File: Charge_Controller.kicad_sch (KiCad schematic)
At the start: 146 parts, among them J1 SOLAR, J10 Conn_01x01_Female, J11 Conn_01x01_Female, J12 Conn_01x01_Female, J13 Conn_01x01_Female, J14 Conn_01x01_Female, J15 Conn_01x01_Female, J16 Conn_01x01_Female, J17 Conn_01x01_Female, J18 Conn_01x01_Female, J19 Conn_01x01_Female, J2 Conn_01x01_Female, J20 Conn_01x01_Female, J21 Conn_01x01_Female, J22 Conn_01x01_Female, J23 Conn_01x01_Female, J24 Conn_01x01_Female, J25 Conn_01x01_Female, J26 Conn_01x01_Female, J27 Conn_01x01_Female, J28 Conn_01x01_Female, J29 Conn_01x01_Female, J3 Conn_01x01_Female, J30 Conn_01x01_Female, J31 Conn_01x01_Female, J32 Conn_01x01_Female, J36 FAN, J37 I2C_CON, J38 I2C_CON, J4 Conn_01x01_Female, J5 Conn_01x01_Female, J6 Conn_01x01_Female, J7 Conn_01x01_Female, J8 BATT, J9 USB_OTG, Q1 CSD19505, Q2 CSD19505, Q3 CSD19505, Q4 Si2306, Q5 2N3904, Q6 2N3904, Q7 PMOS-100V-78A, Q8 PMOS-100V-78A, Q9 Si2306, SW1 RIGHT, SW2 LEFT, SW3 BACK, SW4 SELECT, U1 ACS712-30A, U10 ADS1015, U11 NUP4202, U2 B1212, U3 AMS1117-5.0, U4 AMS1117-3.3, U5 XL7005A, U6 XL7005A, U7 IR2104, U8 ESP32-WROOM-32, U9 CH340C

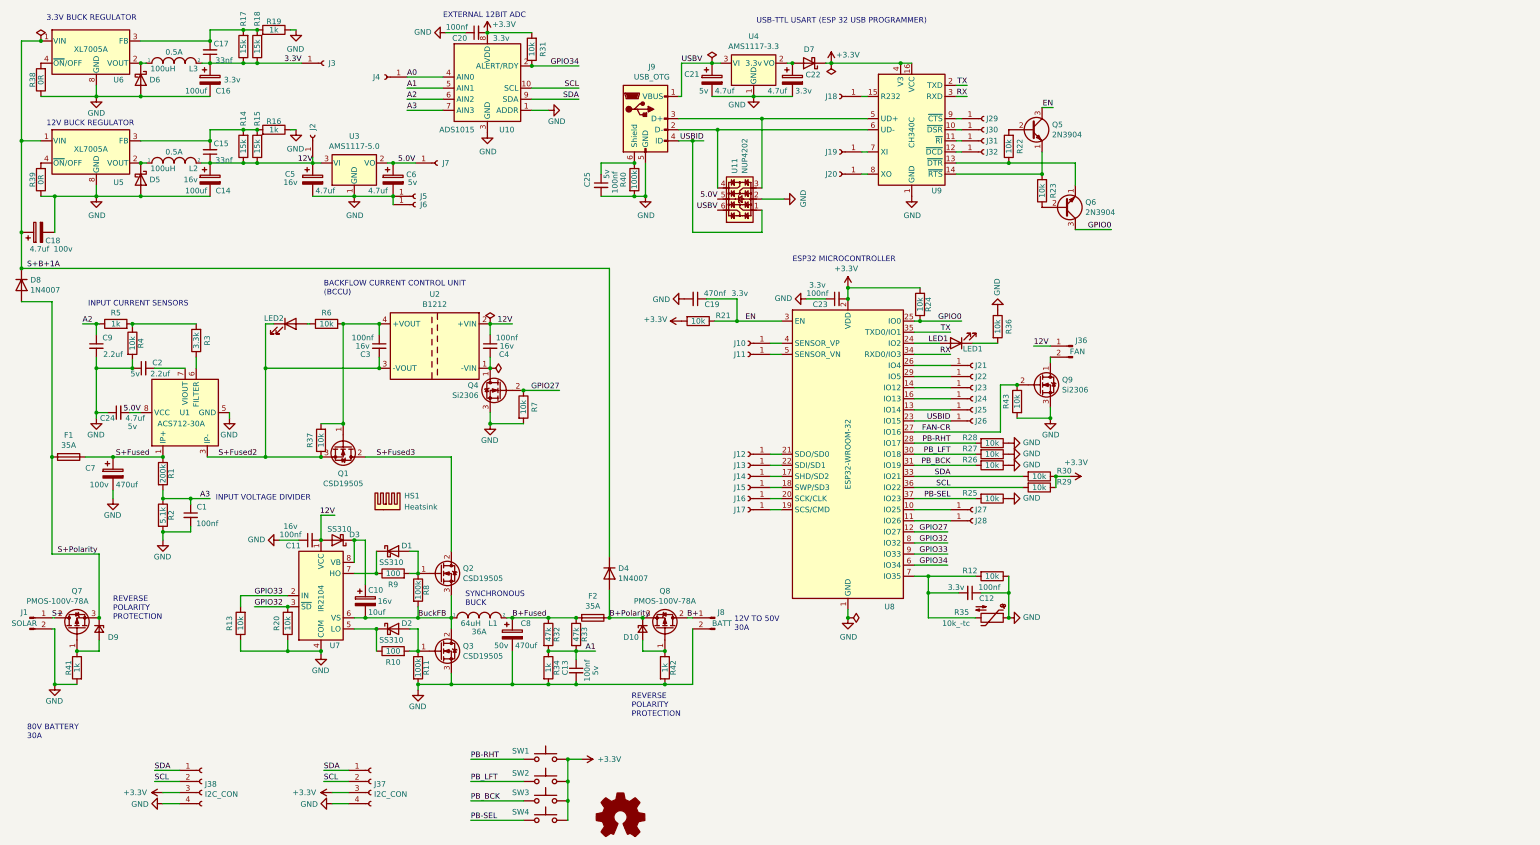
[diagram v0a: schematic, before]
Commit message: Draft adding I2C to LCD driver.
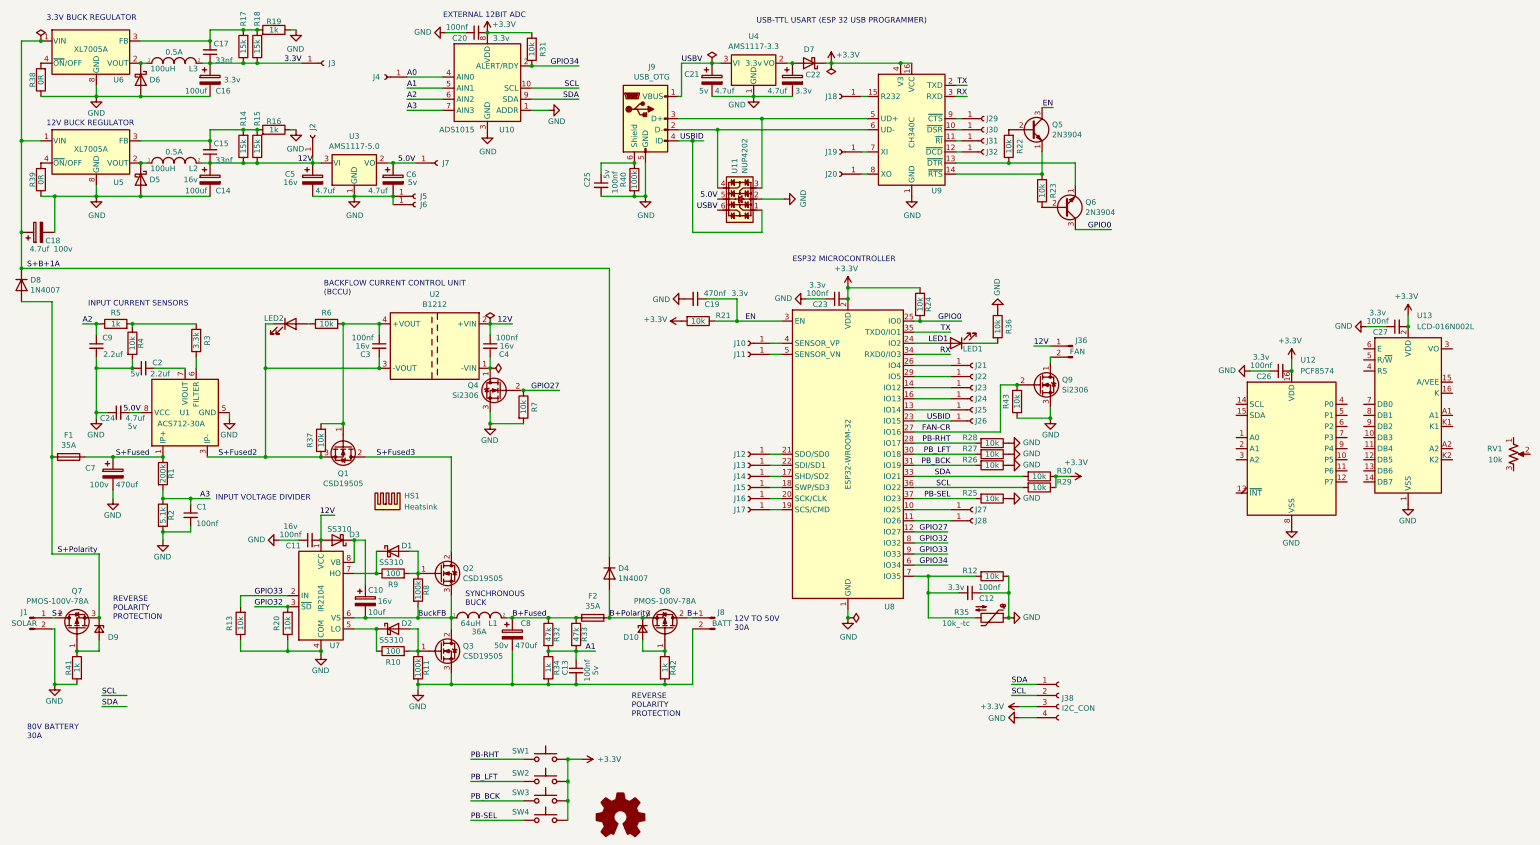
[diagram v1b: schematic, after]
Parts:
- removed J37: I2C_CON, Connector_PinHeader_2.54mm:PinHeader_1x04_P2.54mm_Vertical, symbol Connector:Conn_01x04_Female
- added C26, C27: 100nf, Capacitor_SMD:C_0805_2012Metric, symbol Device:C_Small
- added RV1: 10k, Potentiometer_SMD:Potentiometer_Bourns_3314G_Vertical, symbol Device:R_Potentiometer_US
- added U12: PCF8574, Package_SO:SSOP-20_4.4x6.5mm_P0.65mm, symbol Interface_Expansion:PCF8574
- added U13: LCD-016N002L, Display:LCD-016N002L, symbol Display_Character:LCD-016N002L
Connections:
- net +3.3VA: now also C26.2, C27.2, U12.16 (VDD), U13.2 (VDD)
- net GND: now also C26.1, C27.1, U12.8 (VSS), U13.1 (VSS)
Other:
- moved on the sheet: J38

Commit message: R0.1 almost done draft.
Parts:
- removed U13: LCD-016N002L, Display:LCD-016N002L, symbol Display_Character:LCD-016N002L
- added DS1: LCD, LCD:LCD_LCM-S01602DTR_A, symbol LCM-S01602DTR_A:LCM-S01602DTR/A
- added J33, J34: Conn_01x01_Female, TestPoint:TestPoint_Loop_D3.50mm_Drill0.9mm_Beaded, symbol Connector:Conn_01x01_Female
- added R46, R47, R48: 10k, Resistor_SMD:R_0805_2012Metric, symbol Device:R
- added R49: 330, Resistor_SMD:R_0805_2012Metric, symbol Device:R
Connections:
- net +3.3VA: now also RV1.3, DS1.2 (VDD), R46.1, R47.1, R48.1, R49.1
- net GND: now also RV1.1, DS1.1 (VSS), DS1.10 (DB3), DS1.16 (K), DS1.7 (DB0), DS1.8 (DB1), DS1.9 (DB2), J33.1 (Pin_1), J34.1 (Pin_1)
- net SCL: now also U12.14 (SCL)
- net SDA: now also U12.15 (SDA)
- net at U12.1 (A0): now also R46.2
- net at U12.10 (P5): now also DS1.12 (DB5)
- net at U12.11 (P6): now also DS1.13 (DB6)
- net at U12.12 (P7): now also DS1.14 (DB7)
- net at U12.2 (A1): now also R47.2
- net at U12.3 (A2): now also R48.2
- net RS: now reaches U12.4 (P0)
- net RS: now also DS1.5 (R/~{W})
- net RW: now reaches U12.5 (P1)
- net RW: now also DS1.4 (RS)
- net E: now reaches U12.6 (P2)
- net E: now also DS1.6 (E)
- net at U12.9 (P4): now also DS1.11 (DB4)
- net at RV1.2: now also DS1.3 (VO)
- new net: DS1.15 (A), R49.2
- no-connect marks 0 -> 2
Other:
- note added: "LCD DRIVER"
- company: (none) -> repo https://github.com/jharvey/Charge_Controller
- moved on the sheet: C12, C19, C20, C21, C22, C23, C25, C26, C27, D7, J10, J11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

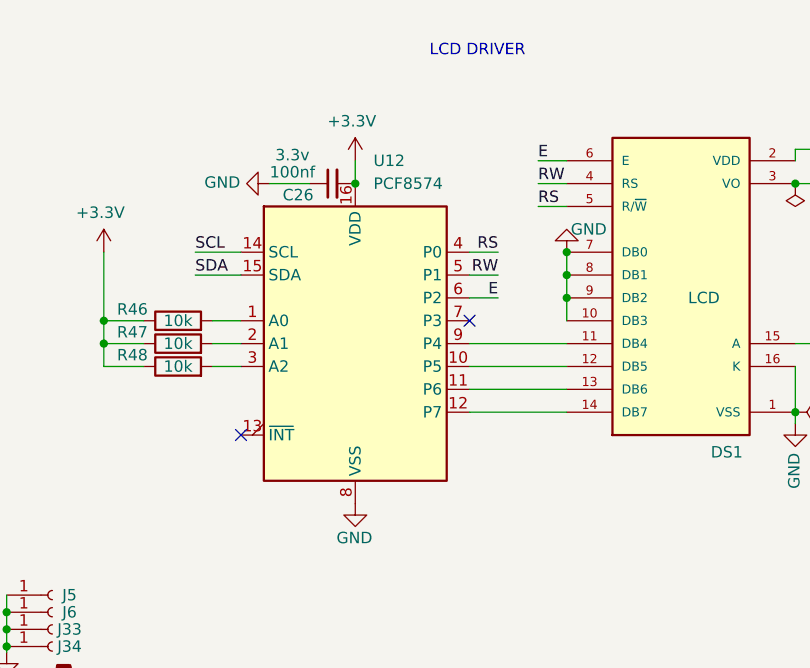
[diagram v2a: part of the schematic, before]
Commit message: Attempting to export a BOM, save before doing something potentially risky.
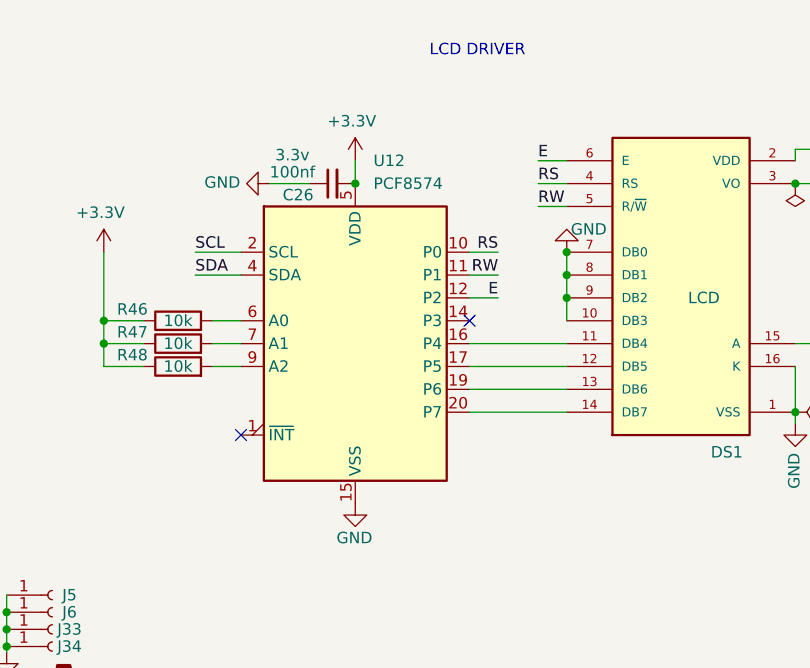
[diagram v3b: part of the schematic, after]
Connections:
- net +3.3VA: now also U12.5 (VDD); no longer U12.16 (VDD)
- net E: now also U12.12 (P2); no longer U12.6 (P2)
- net GND: now also U12.15 (VSS); no longer U12.8 (VSS)
- net RS: now also DS1.4 (RS), U12.10 (P0); no longer DS1.5 (R/~{W}), U12.4 (P0)
- net RW: now also DS1.5 (R/~{W}), U12.11 (P1); no longer DS1.4 (RS), U12.5 (P1)
- net SCL: now also U12.2 (SCL); no longer U12.14 (SCL)
- net SDA: now also U12.4 (SDA); no longer U12.15 (SDA)
- net at DS1.11 (DB4): now also U12.16 (P4); no longer U12.9 (P4)
- net at DS1.12 (DB5): now also U12.17 (P5); no longer U12.10 (P5)
- net at DS1.13 (DB6): now also U12.19 (P6); no longer U12.11 (P6)
- net at DS1.14 (DB7): now also U12.20 (P7); no longer U12.12 (P7)
- net at R47.2: now also U12.7 (A1); no longer U12.2 (A1)
- net at R48.2: now also U12.9 (A2); no longer U12.3 (A2)
- net at U12.1 (~{INT}): no longer R46.2
- new net: R46.2, U12.6 (A0)
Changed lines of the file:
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@@
     (effects (font (size 1.27 1.27)) (justify right bottom))
   )
-  (label "RS" (at 281.94 140.97 0)
+  (label "RS" (at 281.94 138.43 0)
     (effects (font (size 1.27 1.27)) (justify left bottom))
   )
@@
     (effects (font (size 1.27 1.27)) (justify left bottom))
   )
-  (label "RW" (at 281.94 138.43 0)
+  (label "RW" (at 281.94 140.97 0)
     (effects (font (size 1.27 1.27)) (justify left bottom))
   )
@@
       (effects (font (size 1.27 1.27)) (justify left))
     )
-    (property "Footprint" "Package_SO:SSOP-20_4.4x6.5mm_P0.65mm" (id 2) (at 261.62 156.21 0)
+    (property "Footprint" "Package_SO:SSOP-20_4.4x6.5mm_P0.65mm" (id 2) (at 261.62 130.81 0)
       (effects (font (size 1.27 1.27)) hide)
     )
-    (property "Datasheet" "http://www.nxp.com/documents/data_sheet/PCF8574_PCF8574A.pdf" (id 3) (at 261.62 156.21 0)
+    (property "Datasheet" "http://www.nxp.com/documents/data_sheet/PCF8574_PCF8574A.pdf" (id 3) (at 261.62 133.35 0)
       (effects (font (size 1.27 1.27)) hide)
     )
@@
       (effects (font (size 1.27 1.27)) hide)
     )
+    (pin "6")
+    (pin "17")
+    (pin "19")
+    (pin "20")
     (pin "1")
+    (pin "2")
+    (pin "4")
+    (pin "5")
+    (pin "7")
+    (pin "9")
     (pin "10")
     (pin "11")
     (pin "12")
-    (pin "13")
     (pin "14")
     (pin "15")
     (pin "16")
-    (pin "2")
-    (pin "3")
-    (pin "4")
-    (pin "5")
-    (pin "6")
-    (pin "7")
-    (pin "8")
-    (pin "9")
   )
   (symbol (lib_id "power:GND") (at 285.115 146.05 0) (mirror x) (unit 1)

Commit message: Potentially going to release this as the first spin.
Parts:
- C1, C11, C12, C13, C20, C23, C25, C26, C27, C3, C4: LCSC (none) -> C28233; jlcpcb C28233 -> (none)
- C10: LCSC (none) -> C15850; jlcpcb C15850 -> (none)
- C14, C16: LCSC (none) -> C445063; jlcpcb C445063 -> (none)
- C15, C17: LCSC (none) -> C53175; jlcpcb C53175 -> (none)
- C18, C7, C8, F1, F2, J1, J10, J11, J12, J13, J14, J15, J16, J17, J18, J19, J2, J20, J21, J22, J23, J24, J25, J26, J27, J28, J29, J3, J30, J31, J32, J33, J34, J36, J4, J5, J6, J7, J8, L1, R35: LCSC (none) -> NA; jlcpcb NA -> (none)
- C19: LCSC (none) -> C13967; jlcpcb C13967 -> (none)
- C2, C9: LCSC (none) -> C49217; jlcpcb C49217 -> (none)
- C21, C22, C24, C5, C6: LCSC (none) -> C1779; jlcpcb C1779 -> (none)
- D1, D2, D3, D5, D6, D7: LCSC (none) -> C15874; jlcpcb C15874 -> (none)
- D10, D9: LCSC (none) -> C8062; jlcpcb C8062 -> (none)
- D4, D8: LCSC (none) -> C727081; jlcpcb C727081 -> (none)
- DS1, J38, LOGO1: LCSC (none) -> NA
- HS1: Digikey (none) -> AE10798-ND; Field4 AE10798-ND -> (none); LCSC (none) -> NA; jlcpcb NA -> (none)
- J9: LCSC (none) -> C136001; jlcpcb C136001 -> (none)
- L2, L3: LCSC (none) -> C88132; jlcpcb C88132 -> (none)
- LED1, LED2: LCSC (none) -> C84256; jlcpcb C84256 -> (none)
- Q1, Q2, Q3: LCSC (none) -> C485534; jlcpcb C485534 -> (none)
- Q4, Q9: LCSC (none) -> C347489; jlcpcb C347489 -> (none)
- Q5, Q6: LCSC (none) -> C18536; jlcpcb C18536 -> (none)
- Q7, Q8: LCSC (none) -> C216784; jlcpcb C216784 -> (none)
- R1: LCSC (none) -> C17539; jlcpcb C17539 -> (none)
- R10, R9: LCSC (none) -> C17408; jlcpcb C17408 -> (none)
- R11, R40, R8: LCSC (none) -> C149504; jlcpcb C149504 -> (none)
- R12, R13, R20, R21, R22, R23, R24, R25, R26, R27, R28, R29, R30, R31, R36, R37, R4, R43, R46, R47, R48, R6, R7: LCSC (none) -> C17724; jlcpcb C17724 -> (none)
- R14, R15, R17, R18: LCSC (none) -> C17475; jlcpcb C17475 -> (none)
- R16, R19, R34, R41, R42, R5: LCSC (none) -> C17513; jlcpcb C17513 -> (none)
- R2: LCSC (none) -> C27834; jlcpcb C27834 -> (none)
- R3: LCSC (none) -> C26010; jlcpcb C26010 -> (none)
- R32, R33: LCSC (none) -> C17713; jlcpcb C17713 -> (none)
- R38, R39: LCSC (none) -> C21189; jlcpcb C21189 -> (none)
- R49: LCSC (none) -> C17630
- RV1: LCSC (none) -> C780220; jlcpcb C780220 -> (none)
- SW1, SW2, SW3, SW4: LCSC (none) -> C318884; jlcpcb C318884 -> (none)
- U1: LCSC (none) -> C9932; jlcpcb C9932 -> (none)
- U10: LCSC (none) -> C193969; jlcpcb C193969 -> (none)
- U11: LCSC (none) -> C89319; jlcpcb C89319 -> (none)
- U12: footprint Package_SO:SSOP-20_4.4x6.5mm_P0.65mm -> Package_SO:SSOP-20_5.3x7.2mm_P0.65mm; LCSC (none) -> C57790; jlcpcb C57790 -> (none)
- U2: LCSC (none) -> C5127060; jlcpcb C5127060 -> (none)
- U3: LCSC (none) -> C6187; jlcpcb C6187 -> (none)
- U4: LCSC (none) -> C6186; jlcpcb C6186 -> (none)
- U5, U6: LCSC (none) -> C50848; jlcpcb C50848 -> (none)
- U7: LCSC (none) -> C2960; jlcpcb C2960 -> (none)
- U8: LCSC (none) -> C701343; jlcpcb C701343 -> (none)
- U9: LCSC (none) -> C84681; jlcpcb C84681 -> (none)

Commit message: Added a Digikey number for the toroid.
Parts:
- L1: Digikey (none) -> 495-5076-ND
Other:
- note added: "6 turns"
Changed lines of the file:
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@@
     (stroke (width 0) (type default) (color 0 0 0 0))
   )
-  (text "SYNCHRONOUS\nBUCK" (at 116.84 149.86 0)
+  (text "SYNCHRONOUS\nBUCK" (at 121.92 148.59 0)
     (effects (font (size 1.27 1.27)) (justify left bottom))
   )
@@
   )
   (text "INPUT CURRENT SENSORS" (at 30.48 81.28 0)
+    (effects (font (size 1.27 1.27)) (justify left bottom))
+  )
+  (text "6 turns" (at 116.205 150.495 0)
     (effects (font (size 1.27 1.27)) (justify left bottom))
   )
@@
       (effects (font (size 1.27 1.27)) hide)
     )
+    (property "Digikey" "495-5076-ND" (id 6) (at 120.015 152.4 0)
+      (effects (font (size 1.27 1.27)) hide)
+    )
